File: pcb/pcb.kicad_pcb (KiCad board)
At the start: 2 copper layers, 68.6 x 53.3 mm, 19 parts, among them P1 Power, P2 Analog, P3 Digital, P4 Digital, P5 CONN_01X01, P6 CONN_01X01, P7 CONN_01X01, P8 CONN_01X01, Q1 TIP120

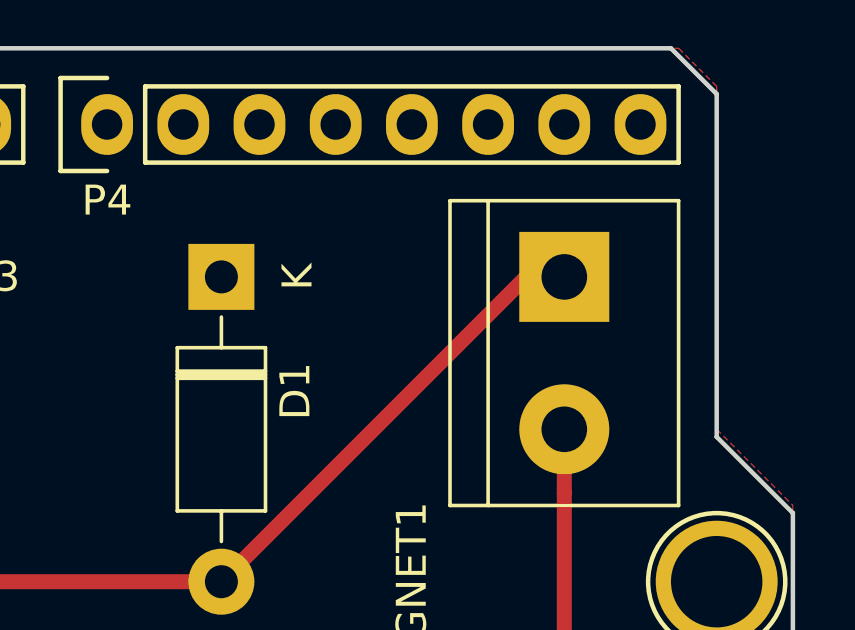
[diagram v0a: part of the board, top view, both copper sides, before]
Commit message: fix sch and pcb bug: diode connect to magnet now
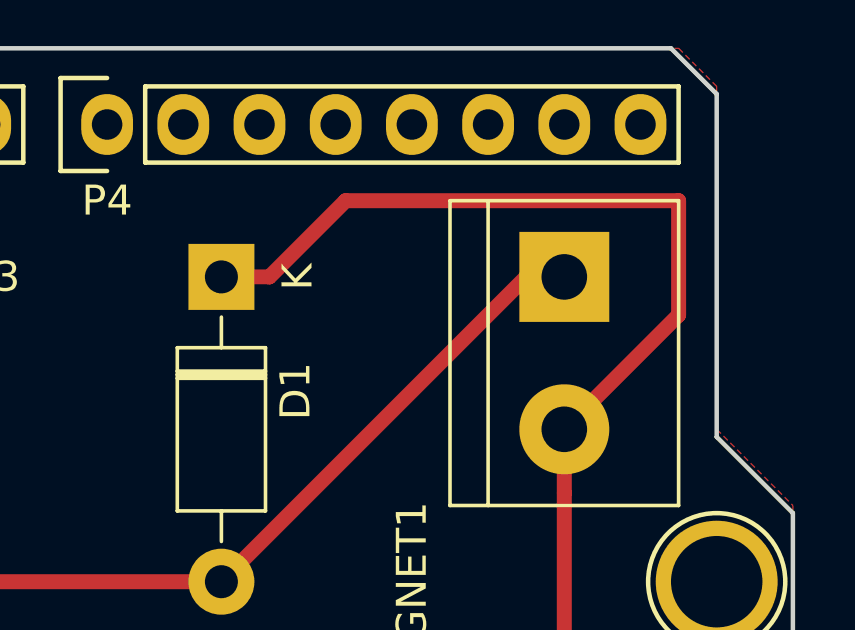
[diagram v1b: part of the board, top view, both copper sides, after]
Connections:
- D1 pad 1: GND -> Net-(D1-Pad1)
- J_ALIM1 pad 1: Net-(J_ALIM1-Pad1) -> Net-(D1-Pad1)
- J_MAGNET1 pad 2: Net-(J_ALIM1-Pad1) -> Net-(D1-Pad1)
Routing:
- net Net-(D1-Pad1): track 0.00 -> 48.0 mm
- net Net-(J_ALIM1-Pad1): track 22.5 -> 0.00 mm
